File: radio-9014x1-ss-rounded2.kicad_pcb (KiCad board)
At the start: 2 copper layers, 95 x 55 mm, 17 parts, among them J1 AudioJack2, Q1 BC547/S9014

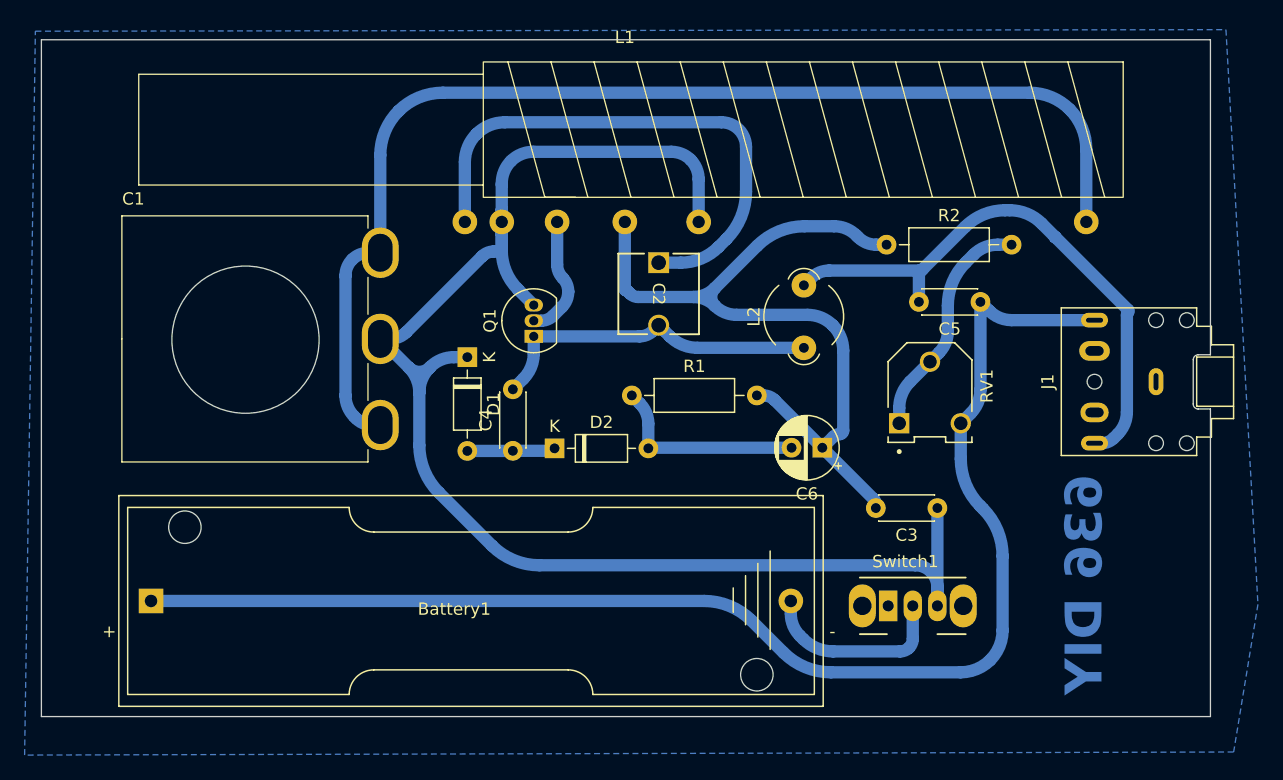
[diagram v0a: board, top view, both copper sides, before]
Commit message: Easier soldering
Edited transistor footprint to the 'wide' variety for easier soldering
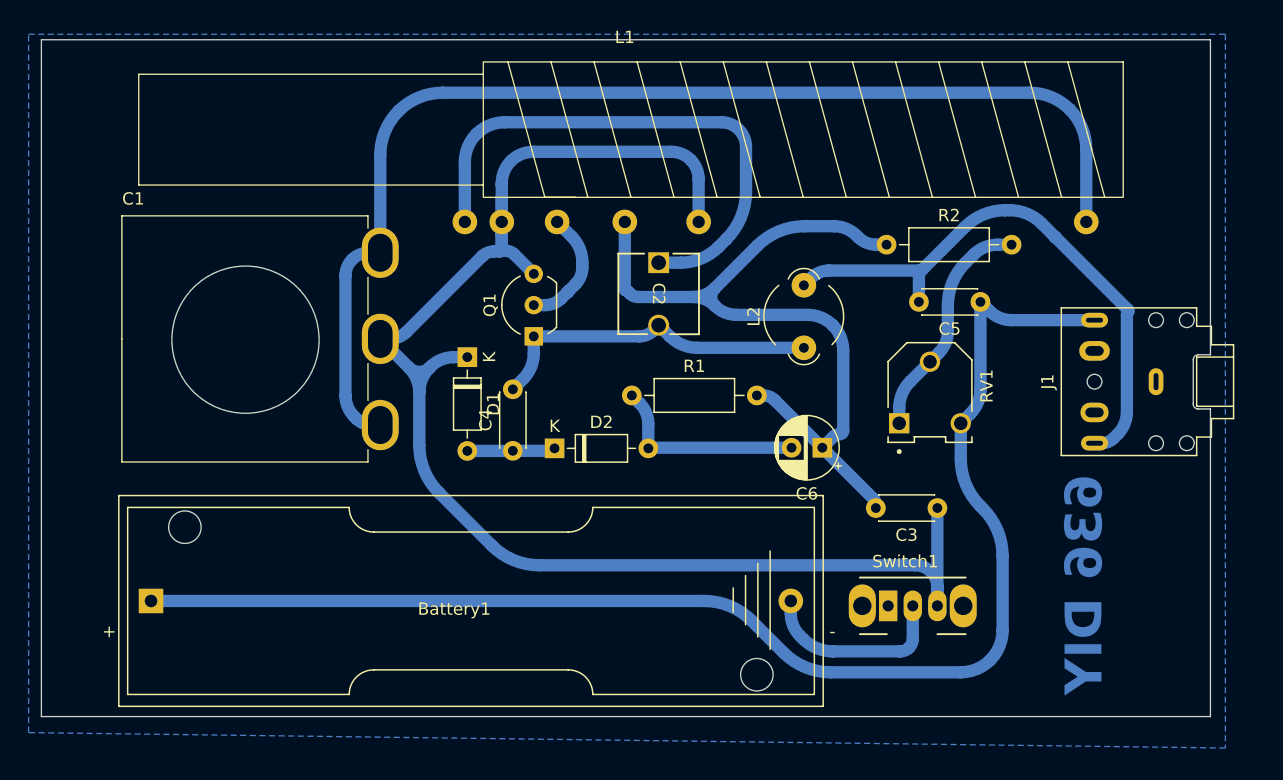
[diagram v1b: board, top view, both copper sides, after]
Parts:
- Q1: footprint Package_TO_SOT_THT:TO-92_Inline -> Package_TO_SOT_THT:TO-92_Inline_Wide
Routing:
- net GND: track 123.5 -> 122.1 mm
- net Net-(Battery1-+): track 110.9 -> 110.2 mm
- added copper zone on B.Cu, net (none)
- removed copper zone on B.Cu, net GND
